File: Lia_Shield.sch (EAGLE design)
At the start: 8 parts, among them U1 HC_05

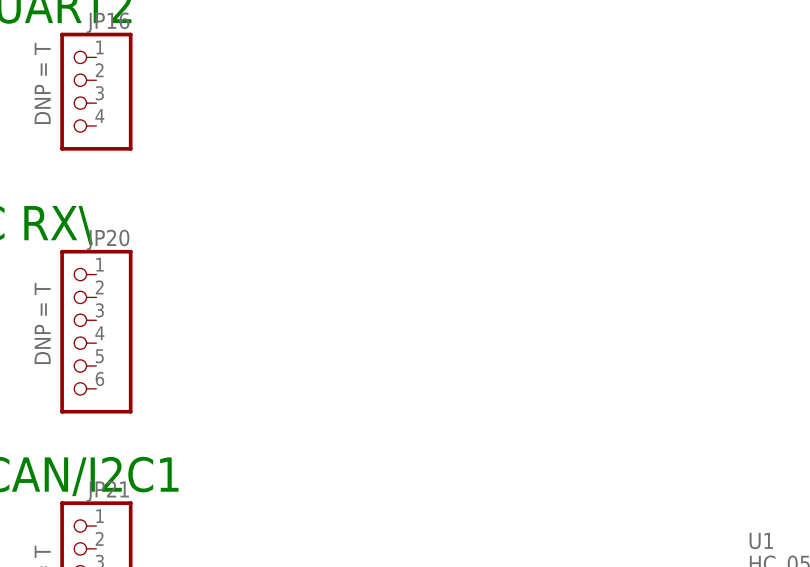
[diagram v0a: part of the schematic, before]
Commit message: angled receiver connector
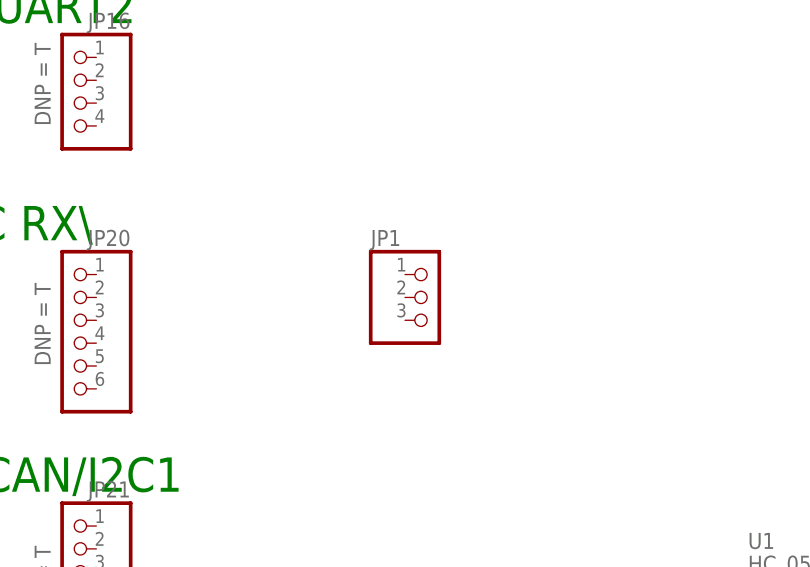
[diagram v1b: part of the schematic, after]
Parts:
- added JP1: (no value), pinhead:PINHD-1X3/90
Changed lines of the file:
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@@
 </part>
 <part name="U1" library="Bluetooth HC-05" deviceset="HC_05" device=""/>
+<part name="JP1" library="pinhead" deviceset="PINHD-1X3" device="/90"/>
 </parts>
 <sheets>
@@
 </instance>
 <instance part="U1" gate="G$1" x="172.72" y="142.24"/>
+<instance part="JP1" gate="A" x="119.38" y="193.04"/>
 </instances>
 <busses>

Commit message: david wollte es so
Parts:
- added JP2, JP3: (no value), pinhead:PINHD-1X6
- added R1, R2: (no value), rcl:R-EU_R1206
- added S1: (no value), SparkFun-Electromechanical:TAC_SWITCHPTH
- added VSENSE: (no value), pinhead:PINHD-1X3/90
- JP21: device pinhead:PINHD-1X7 -> pinhead:PINHD-1X3
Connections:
- new net GND: R1.1
- new net N$1: JP21.2, VSENSE.1
- new net N$10: JP14.3, JP3.3, R2.2
- new net N$11: JP14.1, JP2.2, JP3.5
- new net N$12: JP14.2, JP2.3, JP3.4
- new net N$13: JP14.4, JP2.5, JP3.2
- new net N$14: JP15.4, JP3.1
- new net N$15: JP22.2, S1.3
- new net N$16: JP15.3, R1.2, S1.2
- new net N$17: JP2.4, R2.1
- new net N$2: JP1.1, JP20.1
- new net N$3: JP21.1, VSENSE.3
- new net N$4: JP17.1, U1.GND
- new net N$5: JP1.2, JP20.2
- new net N$6: JP1.3, JP20.3
- new net N$7: JP17.2, U1.3V3
- new net N$8: JP17.3, U1.RX
- new net N$9: JP17.4, U1.TX
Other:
- moved on the sheet: JP14, JP15, JP17, JP20, JP22

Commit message: comitting scheiß
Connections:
- removed net N$11: JP14.1, JP2.2, JP3.5
- removed net N$12: JP14.2, JP2.3, JP3.4
- removed net N$15: JP22.2, S1.3
- removed net N$2 (its old number): JP1.1, JP20.1
- removed net N$3: JP21.1, VSENSE.3
- removed net N$4: JP17.1, U1.GND
- removed net N$5: JP1.2, JP20.2
- removed net N$7: JP17.2, U1.3V3
- new net RC1: JP14.1, JP17.1, JP2.2, JP21.1, JP3.5, R1.1, U1.GND, VSENSE.3
- new net VCC: JP1.2, JP14.2, JP16.2, JP17.2, JP2.3, JP20.2, JP20.5, JP22.2, JP3.4, S1.3, U1.3V3
- net GND: now also JP1.1, JP20.1, JP20.4; no longer R1.1
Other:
- moved on the sheet: JP1, JP16
